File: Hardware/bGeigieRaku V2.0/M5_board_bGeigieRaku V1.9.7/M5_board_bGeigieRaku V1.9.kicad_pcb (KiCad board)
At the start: 2 copper layers, 129.4 x 64.6 mm, 30 parts, among them J1 M5 2x15 pin, J10 QI GND, J11 QI charger Plus, J2 Geiger, J3 GPS, J4 Geiger 2, J7 Conn_01x14_Female, J8 QI charger GND, J9 QI Plus, Q1 IRF4905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

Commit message: Added information for M5Stack pin headers
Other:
- board text added: "2021-03-09 for V1.9.7 - check power track width - realign the holes for M5Stack mounts - check alignments all holes 2021-03-13 - pin headers for M5Stack are Hirosugi Instruments: PSM-4200233-15"
- board text removed: "Notes 2021-03-09 for V1.9.7 - check power track width - realign the holes for M5Stack mounts - check alignments all holes"
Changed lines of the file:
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@@
     (effects (font (size 0.75 0.75) (thickness 0.15)))
   )
-  (gr_text " Notes 2021-03-09 for V1.9.7\n- check power track width\n- realign the holes for M5Stack mounts\n- check alignments all holes\n\n" (at 222.3776 146.44) (layer "Eco2.User")
+  (gr_text "2021-03-09 for V1.9.7\n- check power track width\n- realign the holes for M5Stack mounts\n- check alignments all holes\n\n2021-03-13\n- pin headers for M5Stack are Hirosugi Instruments: PSM-4200233-15\n\n\n" (at 222.3776 146.44) (layer "Eco2.User")
     (effects (font (size 1.5 1.5) (thickness 0.3)) (justify left))
   )

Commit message: Update V1.9.7 board.
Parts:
- added J5: Extra support header, Connector_PinHeader_2.54mm:PinHeader_1x02_P2.54mm_Vertical, F.Cu at (159.5, 106.9)
- D1, D2: value DIODE -> 1N4001; footprint Diode_THT:D_DO-15_P15.24mm_Horizontal -> Diode_THT:D_DO-41_SOD81_P10.16mm_Horizontal
- J3: footprint Connector_PinSocket_2.54mm:PinSocket_1x06_P2.54mm_Vertical -> Connector_PinHeader_2.54mm:PinHeader_1x06_P2.54mm_Vertical
- Q1, Q2: value IRF4905 -> IRFR9024; footprint Package_TO_SOT_THT:TO-220-3_Vertical -> Package_TO_SOT_THT:TO-251-3_Vertical; moved to F.Cu
- moved D2 16.7 mm to (166.6, 82.7)
- moved D1 16.5 mm to (162.7, 82.8)
- moved J7 10.5 mm to (165.9, 108.4)
- moved J4 7.46 mm to (191.1, 90.5)
- moved Q1 4.87 mm to (154.4, 77.2), turned to 90 degrees
- moved Q2 2.51 mm to (158.2, 77.2), turned to 90 degrees
- moved J3 1.35 mm to (153.7, 103.2)
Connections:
- D1 pad 2: /VBATT -> Net-(J11-Pad1)
- D2 pad 1: Net-(D2-Pad1) -> /VBATT
- J11 pad 1: Net-(D2-Pad1) -> Net-(J11-Pad1)
- J11 pad 2: Net-(D2-Pad1) -> Net-(J11-Pad1)
- Q1 pad 2: Net-(D2-Pad1) -> Net-(J11-Pad1)
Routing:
- net Net-(D2-Pad1): track 59.8 -> 0.00 mm
- net Net-(J11-Pad1): track 0.00 -> 55.3 mm
- net /GIO2: track 106.1 -> 117.3 mm
- net /SDA: track 51.6 -> 62.8 mm, vias 0 -> 1
- net 5V: track 56.2 -> 67.1 mm
- net /TX1: track 44.0 -> 54.0 mm
- net /RX1: track 43.5 -> 53.1 mm, vias 0 -> 1
- net 3.3V: track 104.3 -> 113.5 mm
- net Net-(J1-Pad29): track 105.6 -> 112.7 mm
- net /Reset: track 80.8 -> 86.1 mm, vias 2 -> 1
- net Net-(BT1-Pad1): track 86.5 -> 91.2 mm
- net /GIO0: track 70.4 -> 73.4 mm
- net /SCL: track 60.4 -> 63.3 mm
- net /VBATT: track 35.6 -> 33.9 mm
- net /TX2: track 40.6 -> 39.4 mm
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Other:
- board text added: "2021-03-09 for V1.9.7 - check power track width - realign the holes for M5Stack mounts - check alignments all holes 2021-03-13 - pin headers for M5Stack are Hirosugi Instruments: PSM-4200233-15 - https://macsbug.wordpress.com/2018/08/19/low-cost-proto-module-of-m5stack-part-2/"
- board text removed: "2021-03-09 for V1.9.7 - check power track width - realign the holes for M5Stack mounts - check alignments all holes 2021-03-13 - pin headers for M5Stack are Hirosugi Instruments: PSM-4200233-15"

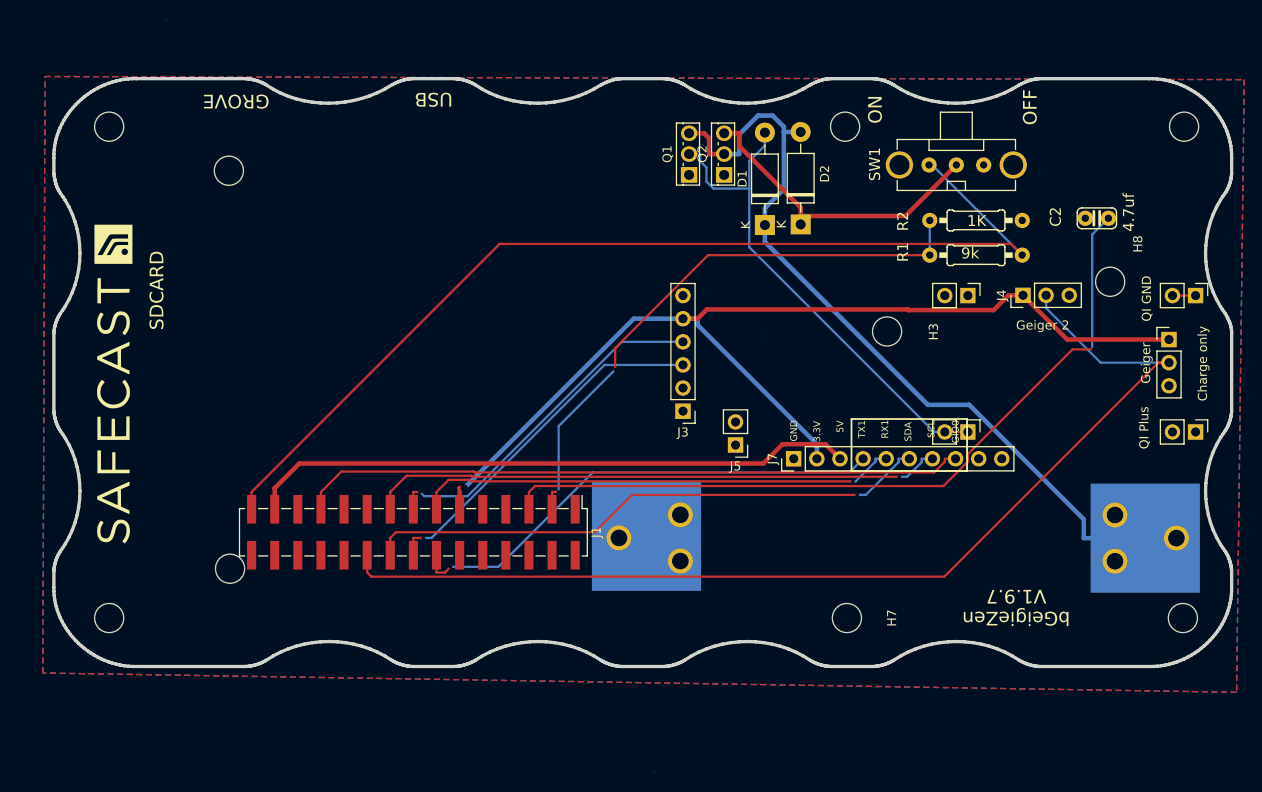
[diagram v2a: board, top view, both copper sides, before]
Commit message: Updated boards. Moved M5stack display 2.1 mm up.
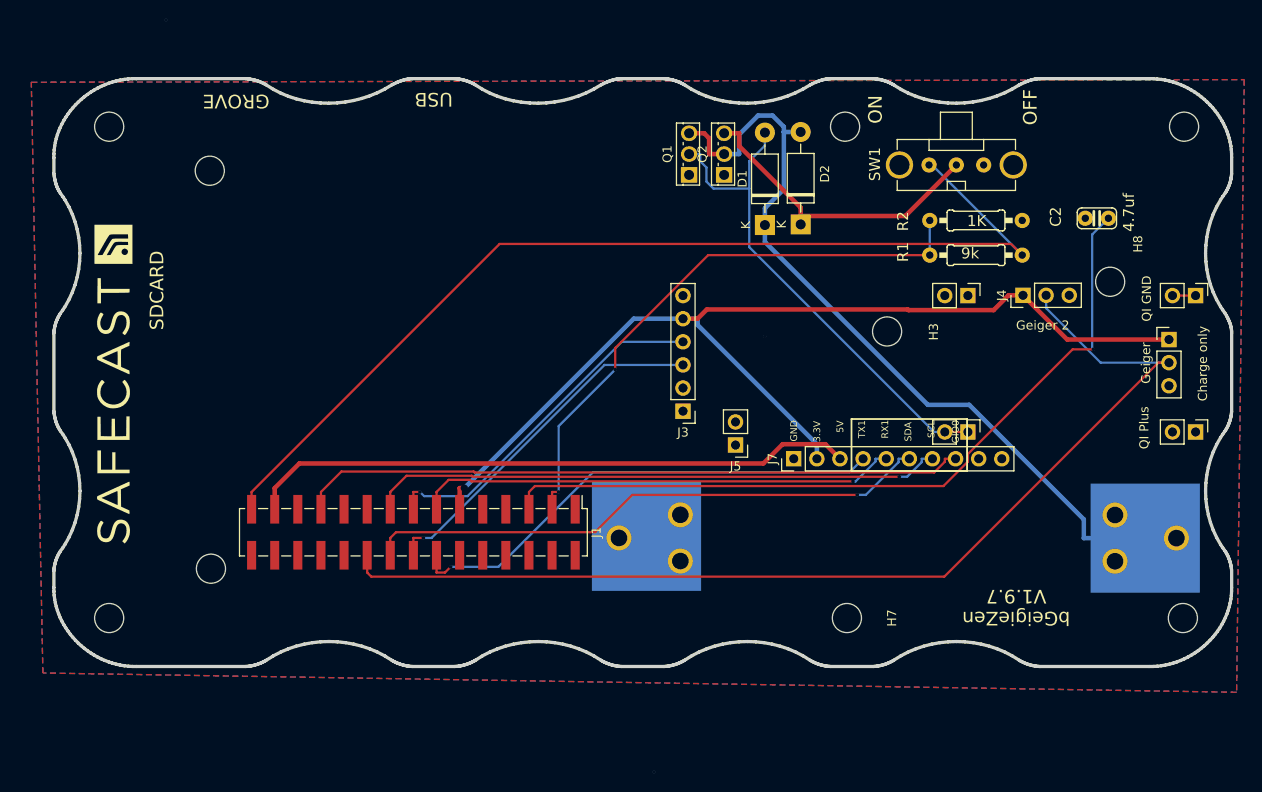
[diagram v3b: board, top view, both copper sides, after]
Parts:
- moved H4 2.10 mm to (101.7, 76.8)
- moved H6 2.10 mm to (101.8, 120.5)
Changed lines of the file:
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@@
   )
   (footprint "MountingHole:MountingHole_3.2mm_M3" (layer "F.Cu")
-    (at 103.808 76.78)
+    (at 101.708 76.78)
     (descr "Mounting Hole 3.2mm, no annular, M3")
     (tags "mounting hole 3.2mm no annular m3")
@@
     (fp_circle (center 0 0) (end 3.45 0) (layer "F.CrtYd") (width 0.05) (fill none))
     (pad "1" np_thru_hole circle (at 0 0) (locked) (size 3.2 3.2) (drill 3.2) (layers *.Cu *.Mask)
-      (net 23 "unconnected-(H4-Pad1)") (pinfunction "1") (pintype "input"))
+      (net 23 "unconnected-(H4-Pad1)") (pinfunction "1"))
   )
   (footprint "MountingHole:MountingHole_3.2mm_M3" (layer "F.Cu")
@@
   )
   (footprint "MountingHole:MountingHole_3.2mm_M3" (layer "F.Cu")
-    (at 103.9376 120.51)
+    (at 101.8376 120.51)
     (descr "Mounting Hole 3.2mm, no annular, M3")
     (tags "mounting hole 3.2mm no annular m3")
@@
     (fp_circle (center 0 0) (end 3.45 0) (layer "F.CrtYd") (width 0.05) (fill none))
     (pad "1" np_thru_hole circle (at 0 0) (locked) (size 3.2 3.2) (drill 3.2) (layers *.Cu *.Mask)
-      (net 35 "unconnected-(H6-Pad1)") (pinfunction "1") (pintype "input"))
+      (net 35 "unconnected-(H6-Pad1)") (pinfunction "1"))
   )
   (footprint "MountingHole:MountingHole_3.2mm_M3" (layer "F.Cu")
@@
         (xy 214.5376 134.09)
         (xy 83.3676 131.97)
-        (xy 83.6076 66.43)
+        (xy 82.0976 67.06)
         (xy 215.3776 66.77)
       )

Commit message: Moved M5stack connector 2.0mm  in -x  direction.
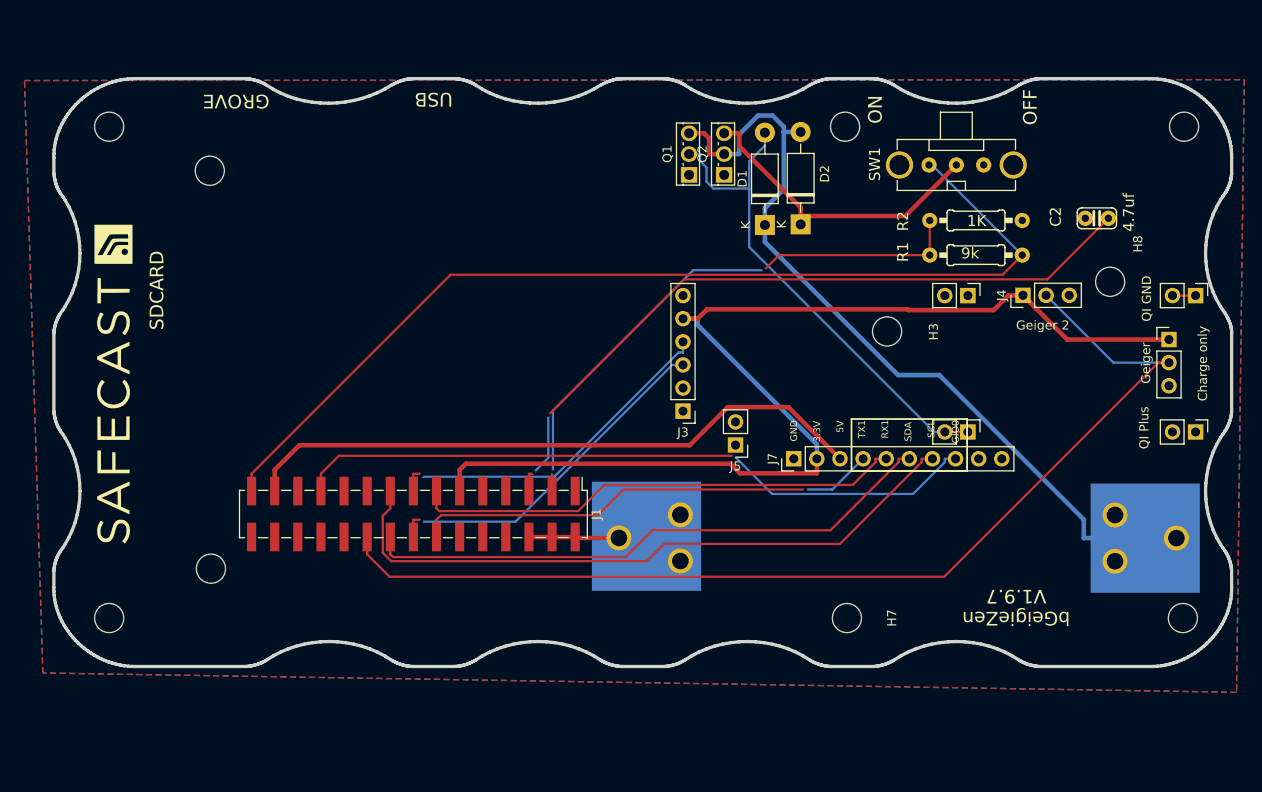
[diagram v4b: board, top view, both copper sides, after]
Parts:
- moved J1 2.00 mm to (124.1, 114.5)
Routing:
- net GND: track 3.11 -> 13.0 mm, vias 1 -> 0
- net /SCL: track 63.3 -> 72.8 mm, vias 1 -> 0
- net 3.3V: track 113.5 -> 122.9 mm, vias 1 -> 0
- net /Reset: track 86.1 -> 80.0 mm, vias 1 -> 2
- net /GIO0: track 73.4 -> 76.0 mm, vias 0 -> 1
- net 5V: track 67.1 -> 69.6 mm
- net Net-(J1-Pad3): track 63.6 -> 61.2 mm
- net /TX1: track 54.0 -> 51.5 mm
- net Net-(J1-Pad29): track 112.7 -> 110.9 mm
- net /SDA: track 62.8 -> 63.7 mm, vias 1 -> 0
- net /RX1: track 53.1 -> 54.0 mm, vias 1 -> 0
- net /TX2: track 39.4 -> 38.7 mm
- net (no net): vias 2 -> 0
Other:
- board text added: "NOTES: 2021-03-09 for V1.9.7 - check power track width - realign the holes for M5Stack mounts - check alignments all holes 2021-03-13 - pin headers for M5Stack are Hirosugi Instruments: PSM-4200233-15 - https://macsbug.wordpress.com/2018/08/19/low-cost-proto-module-of-m5stack-part-2/ 2021-03-16 - moved M5Stack connector y -2.0 mm - moved mounting holes M5Stack x -2.1 mm"
- board text removed: "2021-03-09 for V1.9.7 - check power track width - realign the holes for M5Stack mounts - check alignments all holes 2021-03-13 - pin headers for M5Stack are Hirosugi Instruments: PSM-4200233-15 - https://macsbug.wordpress.com/2018/08/19/low-cost-proto-module-of-m5stack-part-2/"

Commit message: Last adjustements for M5stack after many cuts.
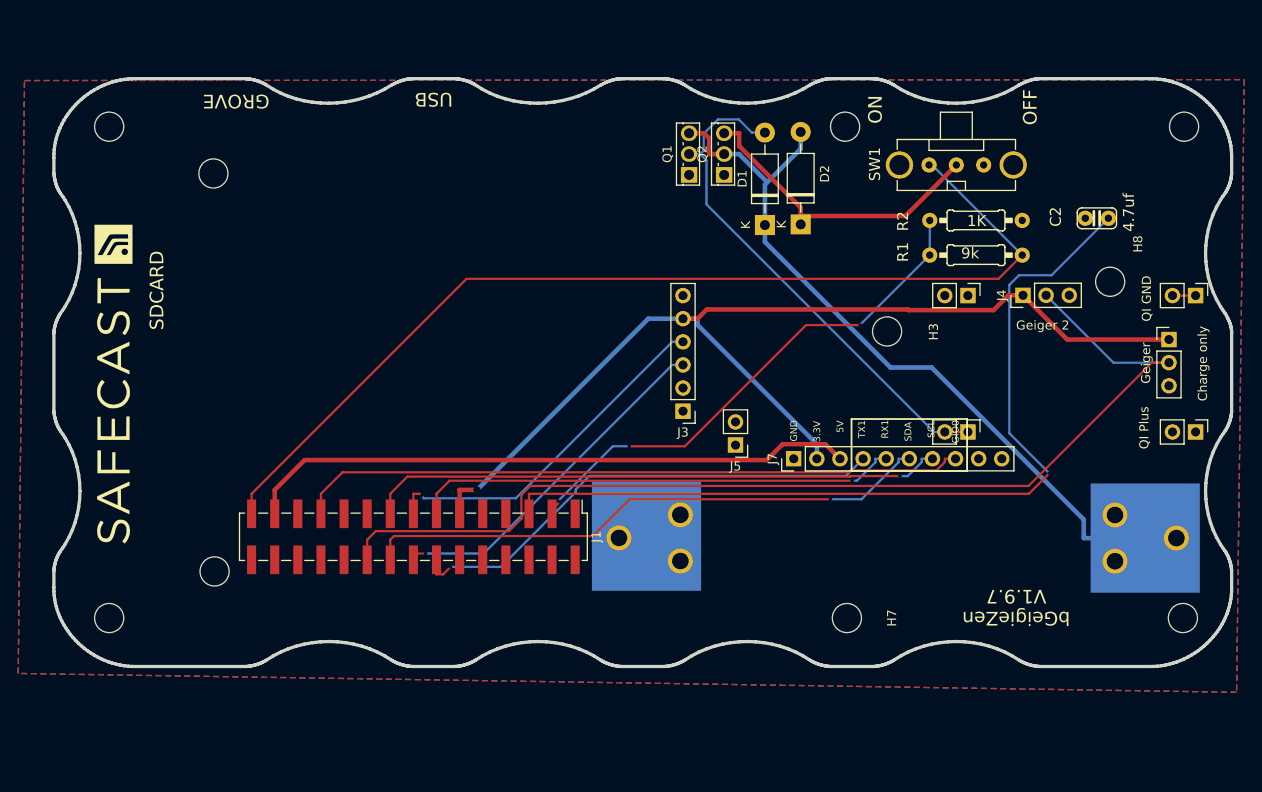
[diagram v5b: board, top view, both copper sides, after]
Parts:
- moved J1 2.50 mm to (124.1, 117.0)
- moved H4 0.50 mm to (102.1, 77.1)
- moved H6 0.50 mm to (102.2, 120.8)
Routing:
- net /Reset: track 80.0 -> 96.5 mm, vias 2 -> 1
- net GND: track 13.0 -> 3.11 mm
- net /SCL: track 72.8 -> 63.3 mm, vias 0 -> 1
- net 3.3V: track 122.9 -> 113.6 mm, vias 0 -> 1
- net Net-(BT1-Pad1): track 91.2 -> 85.4 mm
- net Net-(J1-Pad3): track 61.2 -> 57.3 mm, vias 2 -> 3
- net /TX1: track 51.5 -> 54.2 mm
- net /GIO0: track 76.0 -> 73.4 mm, vias 1 -> 0
- net 5V: track 69.6 -> 67.2 mm
- net Net-(J11-Pad1): track 55.3 -> 56.5 mm
- net /GIO2: track 117.3 -> 116.2 mm
- net /SDA: track 63.7 -> 62.8 mm, vias 0 -> 1
- net /RX1: track 54.0 -> 53.1 mm, vias 0 -> 1
- net Net-(J1-Pad29): track 110.9 -> 111.8 mm

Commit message: Remove  Q1 and D1 (mosfet proteting TP4056)
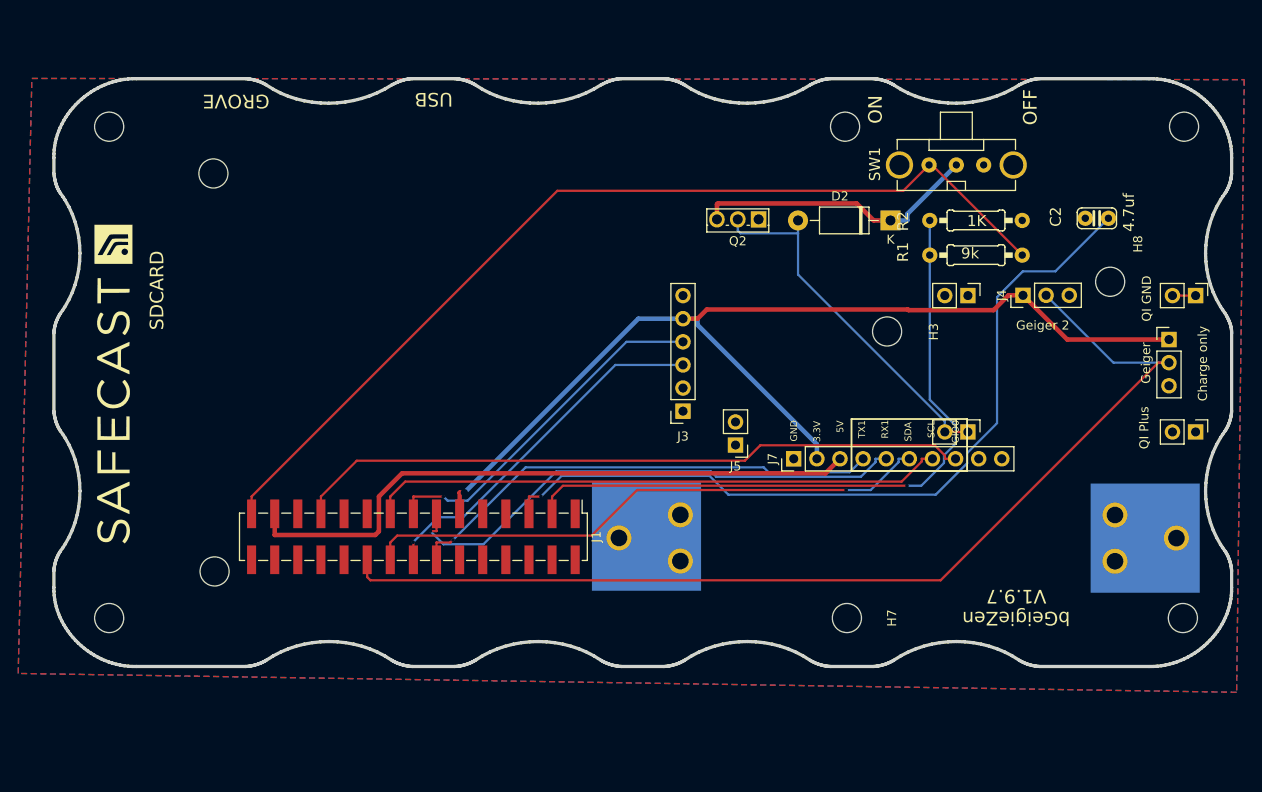
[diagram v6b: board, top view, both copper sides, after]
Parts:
- removed D1: 1N4001, Diode_THT:D_DO-41_SOD81_P10.16mm_Horizontal
- removed Q1: IRFR9024, Package_TO_SOT_THT:TO-251-3_Vertical
- J3: footprint Connector_PinHeader_2.54mm:PinHeader_1x06_P2.54mm_Vertical -> Connector_PinSocket_2.54mm:PinSocket_1x06_P2.54mm_Vertical
- moved D2 9.88 mm to (176.5, 82.2), turned to 180 degrees
- moved Q2 6.18 mm to (162.0, 82.1), turned to 180 degrees
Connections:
- D2 pad 2: Net-(BT1-Pad1) -> Net-(J11-Pad1)
- Q2 pad 2: Net-(BT1-Pad1) -> Net-(J11-Pad1)
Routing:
- net Net-(BT1-Pad1): track 85.4 -> 3.43 mm
- net Net-(J1-Pad3): track 57.3 -> 74.9 mm, vias 3 -> 1
- net Net-(J11-Pad1): track 56.5 -> 40.4 mm
- net /Reset: track 96.5 -> 88.7 mm
- net Net-(J1-Pad29): track 111.8 -> 105.8 mm
- net /RX1: track 53.1 -> 57.9 mm
- net 5V: track 67.2 -> 70.2 mm
- net /VBATT: track 33.9 -> 31.7 mm
- net /GIO0: track 73.4 -> 74.8 mm
- net /TX2: track 38.4 -> 39.7 mm
- net /TX1: track 54.2 -> 53.0 mm
- net /SCL: track 63.3 -> 63.4 mm, vias 1 -> 0

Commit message: Moved display 1mm to the left to get it centered.
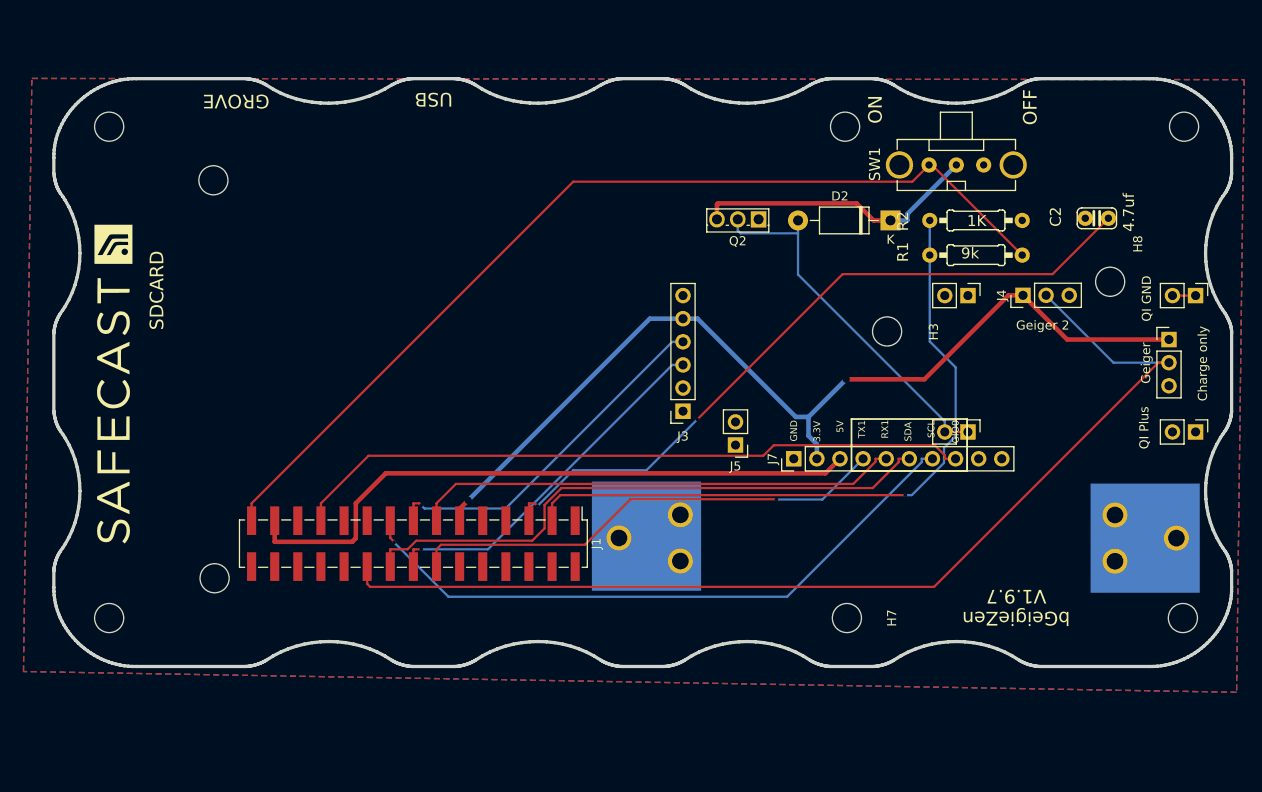
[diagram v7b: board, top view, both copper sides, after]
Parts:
- moved H4 0.75 mm to (102.1, 77.8)
- moved H6 0.75 mm to (102.2, 121.6)
- moved J1 0.75 mm to (124.1, 117.8)
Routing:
- net /Reset: track 88.7 -> 78.8 mm, vias 1 -> 2
- net 3.3V: track 113.7 -> 104.9 mm, vias 1 -> 2
- net /SCL: track 63.4 -> 70.7 mm, vias 0 -> 1
- net /RX1: track 57.9 -> 53.5 mm, vias 1 -> 0
- net /SDA: track 63.0 -> 64.8 mm, vias 1 -> 0
